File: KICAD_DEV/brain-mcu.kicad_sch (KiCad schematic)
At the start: 14 parts, among them SW1 SW_Push, U1 STM32H743VITx

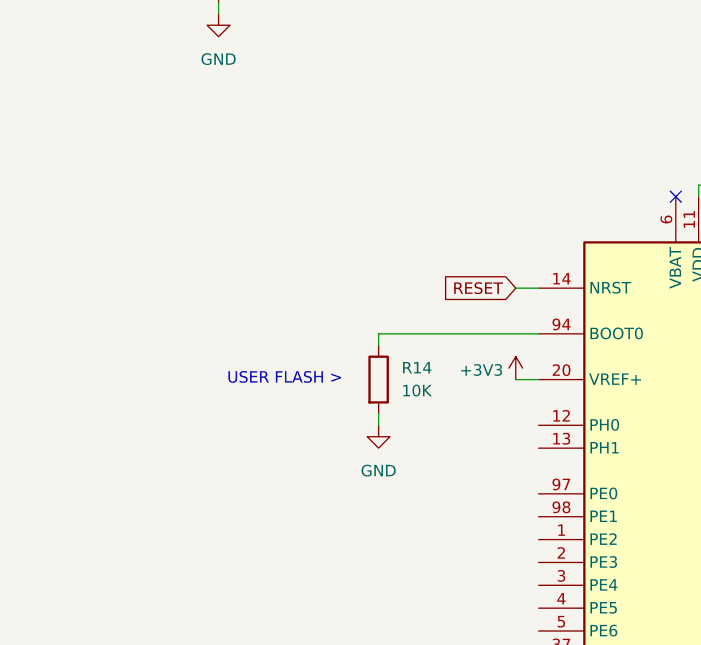
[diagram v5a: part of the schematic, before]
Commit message: added the boot button
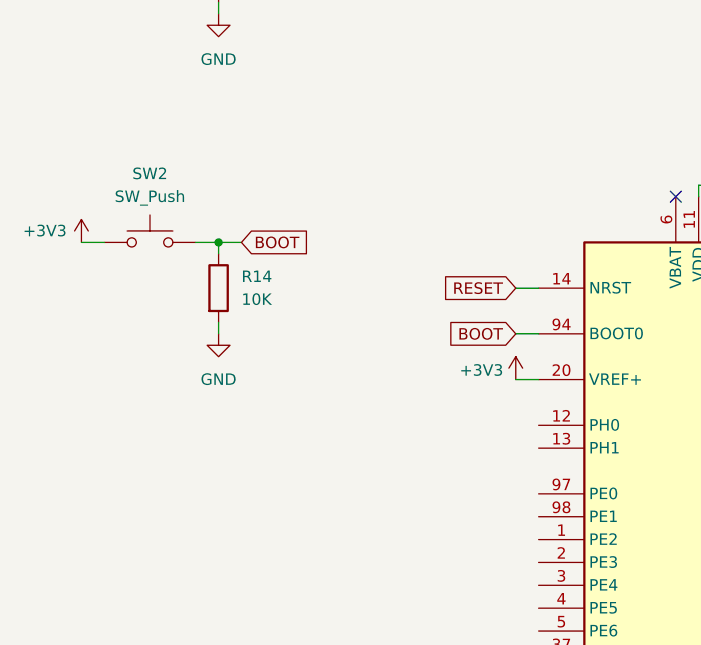
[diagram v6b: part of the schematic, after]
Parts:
- added SW2: SW_Push, symbol Switch:SW_Push
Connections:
- net +3V3: now also SW2.1
- net BOOT: now reaches R14.1, U1.94 (BOOT0)
- net BOOT: now also SW2.2
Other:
- note removed: "USER FLASH >"
- moved on the sheet: R14
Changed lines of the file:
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@@
 	(generator_version "9.0")
 	(paper "A3")
-	(text "USER FLASH >"
-		(exclude_from_sim no)
-		(at 171.196 111.76 0)
-		(effects
-			(font
-				(size 1.27 1.27)
-			)
-		)
-	)
 	(junction
 		(at 219.71 90.17)
@@
 		(color 0 0 0 0)
 	)
+	(junction
+		(at 163.83 96.52)
+		(diameter 0)
+		(color 0 0 0 0)
+	)
 	(no_connect
 		(at 214.63 91.44)
@@
 	(wire
 		(pts
+			(xy 148.59 96.52) (xy 151.13 96.52)
+		)
+		(stroke
+			(width 0)
+			(type default)
+		)
+	)
+	(wire
+		(pts
 			(xy 198.12 210.82) (xy 199.39 210.82)
 		)
@@
 	(wire
 		(pts
-			(xy 181.61 107.95) (xy 181.61 106.68)
+			(xy 163.83 97.79) (xy 163.83 96.52)
 		)
 		(stroke
@@
 	(wire
 		(pts
-			(xy 181.61 106.68) (xy 199.39 106.68)
-		)
-		(stroke
-			(width 0)
-			(type default)
-		)
-	)
-	(wire
-		(pts
 			(xy 208.28 55.88) (xy 208.28 57.15)
 		)
@@
 	(wire
 		(pts
+			(xy 196.85 106.68) (xy 199.39 106.68)
+		)
+		(stroke
+			(width 0)
+			(type default)
+		)
+	)
+	(wire
+		(pts
 			(xy 238.76 55.88) (xy 238.76 57.15)
 		)
@@
 	(wire
 		(pts
+			(xy 161.29 96.52) (xy 163.83 96.52)
+		)
+		(stroke
+			(width 0)
+			(type default)
+		)
+	)
+	(wire
+		(pts
 			(xy 148.59 60.96) (xy 151.13 60.96)
 		)
@@
 	(wire
 		(pts
+			(xy 163.83 96.52) (xy 166.37 96.52)
+		)
+		(stroke
+			(width 0)
+			(type default)
+		)
+	)
+	(wire
+		(pts
 			(xy 223.52 53.34) (xy 223.52 55.88)
 		)
@@
 	(wire
 		(pts
-			(xy 181.61 116.84) (xy 181.61 115.57)
+			(xy 163.83 106.68) (xy 163.83 105.41)
 		)
 		(stroke
@@
 		)
 	)
+	(global_label "BOOT"
+		(shape input)
+		(at 166.37 96.52 0)
+		(fields_autoplaced yes)
+		(effects
+			(font
+				(size 1.27 1.27)
+			)
+			(justify left)
+		)
+		(property "Intersheetrefs" "${INTERSHEET_REFS}"
+			(at 174.2538 96.52 0)
+			(effects
+				(font
+					(size 1.27 1.27)
+				)
+				(justify left)
+				(hide yes)
+			)
+		)
+	)
+	(global_label "BOOT"
+		(shape input)
+		(at 196.85 106.68 180)
+		(fields_autoplaced yes)
+		(effects
+			(font
+				(size 1.27 1.27)
+			)
+			(justify right)
+		)
+		(property "Intersheetrefs" "${INTERSHEET_REFS}"
+			(at 188.9662 106.68 0)
+			(effects
+				(font
+					(size 1.27 1.27)
+				)
+				(justify right)
+				(hide yes)
+			)
+		)
+	)
 	(symbol
 		(lib_id "Device:C")
@@
 	)
 	(symbol
+		(lib_id "power:+3V3")
+		(at 148.59 96.52 0)
+		(unit 1)
+		(exclude_from_sim no)
+		(in_bom yes)
+		(on_board yes)
+		(dnp no)
+		(property "Reference" "#PWR043"
+			(at 148.59 100.33 0)
+			(effects
+				(font
+					(size 1.27 1.27)
+				)
+				(hide yes)
+			)
+		)
+		(property "Value" "+3V3"
+			(at 144.526 95.25 0)
+			(effects
+				(font
+					(size 1.27 1.27)
+				)
+			)
+		)
+		(property "Footprint" ""
+			(at 148.59 96.52 0)
+			(effects
+				(font
+					(size 1.27 1.27)
+				)
+				(hide yes)
+			)
+		)
+		(property "Datasheet" ""
+			(at 148.59 96.52 0)
+			(effects
+				(font
+					(size 1.27 1.27)
+				)
+				(hide yes)
+			)
+		)
+		(property "Description" "Power symbol creates a global label with name \"+3V3\""
+			(at 148.59 96.52 0)
+			(effects
+				(font
+					(size 1.27 1.27)
+				)
+				(hide yes)
+			)
+		)
+		(pin "1"
+		)
+		(instances
+			(project ""
+				(path "/28389848-e686-45d1-8788-e912d76b51d3/e89d2a57-06d5-4f43-8b58-178aa33298cf"
+					(reference "#PWR043")
+					(unit 1)
+				)
+			)
+		)
+	)
+	(symbol
 		(lib_id "Switch:SW_Push")
 		(at 156.21 60.96 0)
@@
 	(symbol
 		(lib_id "Device:R")
-		(at 181.61 111.76 0)
+		(at 163.83 101.6 0)
 		(unit 1)
 		(exclude_from_sim no)
@@
 		(fields_autoplaced yes)
 		(property "Reference" "R14"
-			(at 184.15 110.4899 0)
+			(at 166.37 100.3299 0)
 			(effects
 				(font
@@
 		)
 		(property "Value" "10K"
-			(at 184.15 113.0299 0)
-			(effects
-				(font
-					(size 1.27 1.27)
-				)
-				(justify left)
-			)
-		)
-		(property "Footprint" ""
-			(at 179.832 111.76 90)
+			(at 166.37 102.8699 0)
+			(effects
+				(font
+					(size 1.27 1.27)
+				)
+				(justify left)
+			)
+		)
+		(property "Footprint" ""
+			(at 162.052 101.6 90)
 			(effects
 				(font
@@
 		)
 		(property "Datasheet" "~"
-			(at 181.61 111.76 0)
+			(at 163.83 101.6 0)
 			(effects
 				(font
@@
 		)
 		(property "Description" "Resistor"
-			(at 181.61 111.76 0)
+			(at 163.83 101.6 0)
 			(effects
 				(font
@@
 	)
 	(symbol
+		(lib_id "Switch:SW_Push")
+		(at 156.21 96.52 0)
+		(unit 1)
+		(exclude_from_sim no)
+		(in_bom yes)
+		(on_board yes)
+		(dnp no)
+		(fields_autoplaced yes)
+		(property "Reference" "SW2"
+			(at 156.21 88.9 0)
+			(effects
+				(font
+					(size 1.27 1.27)
+				)
+			)
+		)
+		(property "Value" "SW_Push"
+			(at 156.21 91.44 0)
+			(effects
+				(font
+					(size 1.27 1.27)
+				)
+			)
+		)
+		(property "Footprint" ""
+			(at 156.21 91.44 0)
+			(effects
+				(font
+					(size 1.27 1.27)
+				)
+				(hide yes)
+			)
+		)
+		(property "Datasheet" "~"
+			(at 156.21 91.44 0)
+			(effects
+				(font
+					(size 1.27 1.27)
+				)
+				(hide yes)
+			)
+		)
+		(property "Description" "Push button switch, generic, two pins"
+			(at 156.21 96.52 0)
+			(effects
+				(font
+					(size 1.27 1.27)
+				)
+				(hide yes)
+			)
+		)
+		(pin "1"
+		)
+		(pin "2"
+		)
+		(instances
+			(project ""
+				(path "/28389848-e686-45d1-8788-e912d76b51d3/e89d2a57-06d5-4f43-8b58-178aa33298cf"
+					(reference "SW2")
+					(unit 1)
+				)
+			)
+		)
+	)
+	(symbol
 		(lib_id "Device:C")
 		(at 223.52 60.96 0)
@@
 	(symbol
 		(lib_id "power:GND")
-		(at 181.61 116.84 0)
+		(at 163.83 106.68 0)
 		(unit 1)
 		(exclude_from_sim no)
@@
 		(fields_autoplaced yes)
 		(property "Reference" "#PWR042"
-			(at 181.61 123.19 0)
+			(at 163.83 113.03 0)
 			(effects
 				(font
@@
 		)
 		(property "Value" "GND"
-			(at 181.61 121.92 0)
-			(effects
-				(font
-					(size 1.27 1.27)
-				)
-			)
-		)
-		(property "Footprint" ""
-			(at 181.61 116.84 0)
+			(at 163.83 111.76 0)
+			(effects
+				(font
+					(size 1.27 1.27)
+				)
+			)
+		)
+		(property "Footprint" ""
+			(at 163.83 106.68 0)
 			(effects
 				(font
@@
 		)
 		(property "Datasheet" ""
-			(at 181.61 116.84 0)
+			(at 163.83 106.68 0)
 			(effects
 				(font
@@
 		)
 		(property "Description" "Power symbol creates a global label with name \"GND\" , ground"
-			(at 181.61 116.84 0)
-			(effects
-				(font
+			(at 163.83 106.68 0)
+			(effects
+				(font

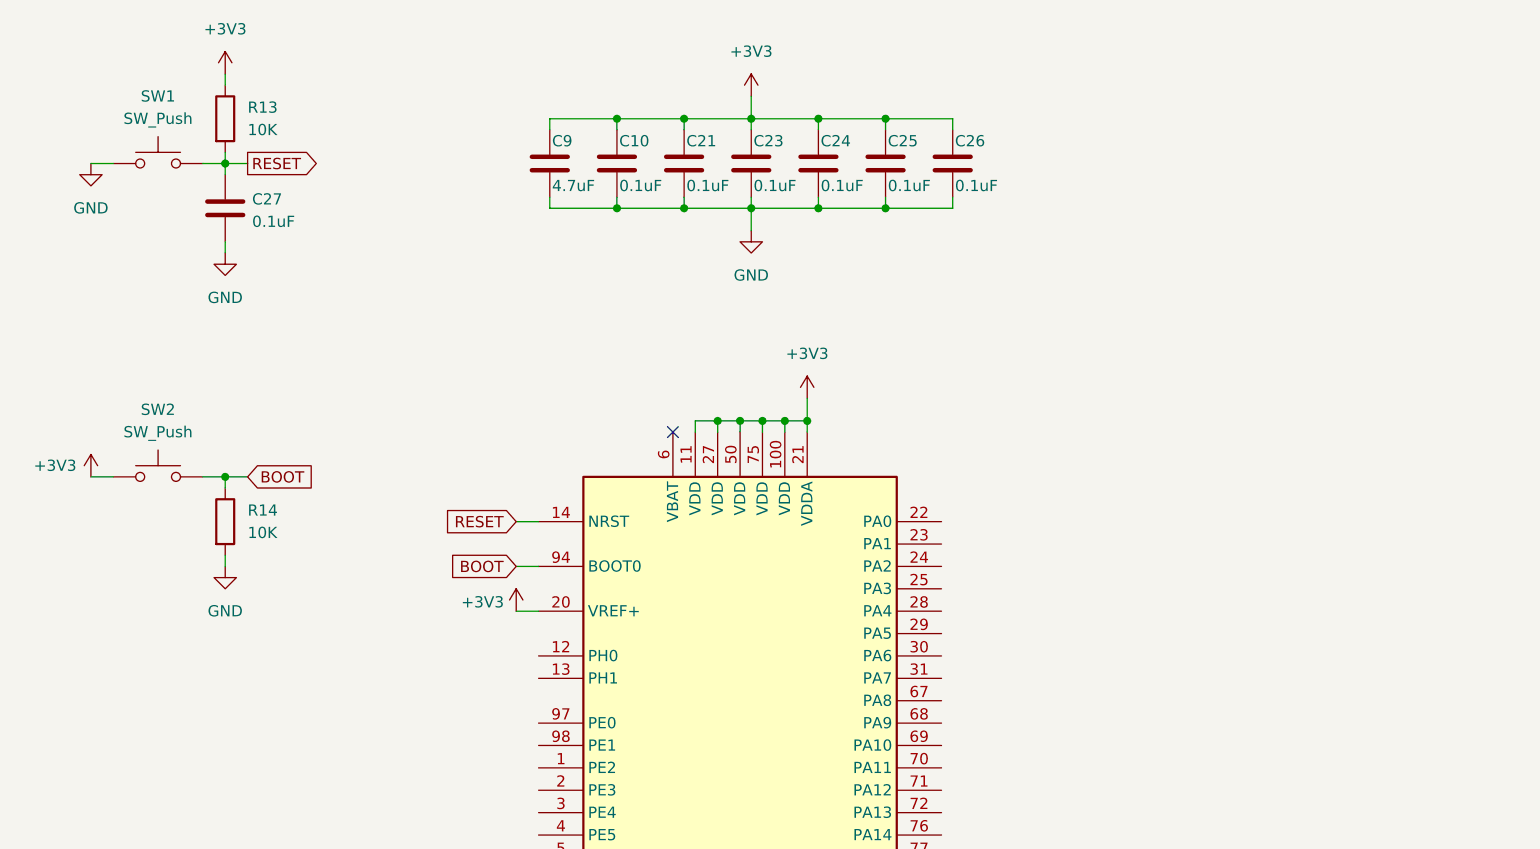
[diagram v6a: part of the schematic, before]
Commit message: adding the 8mhz crystal
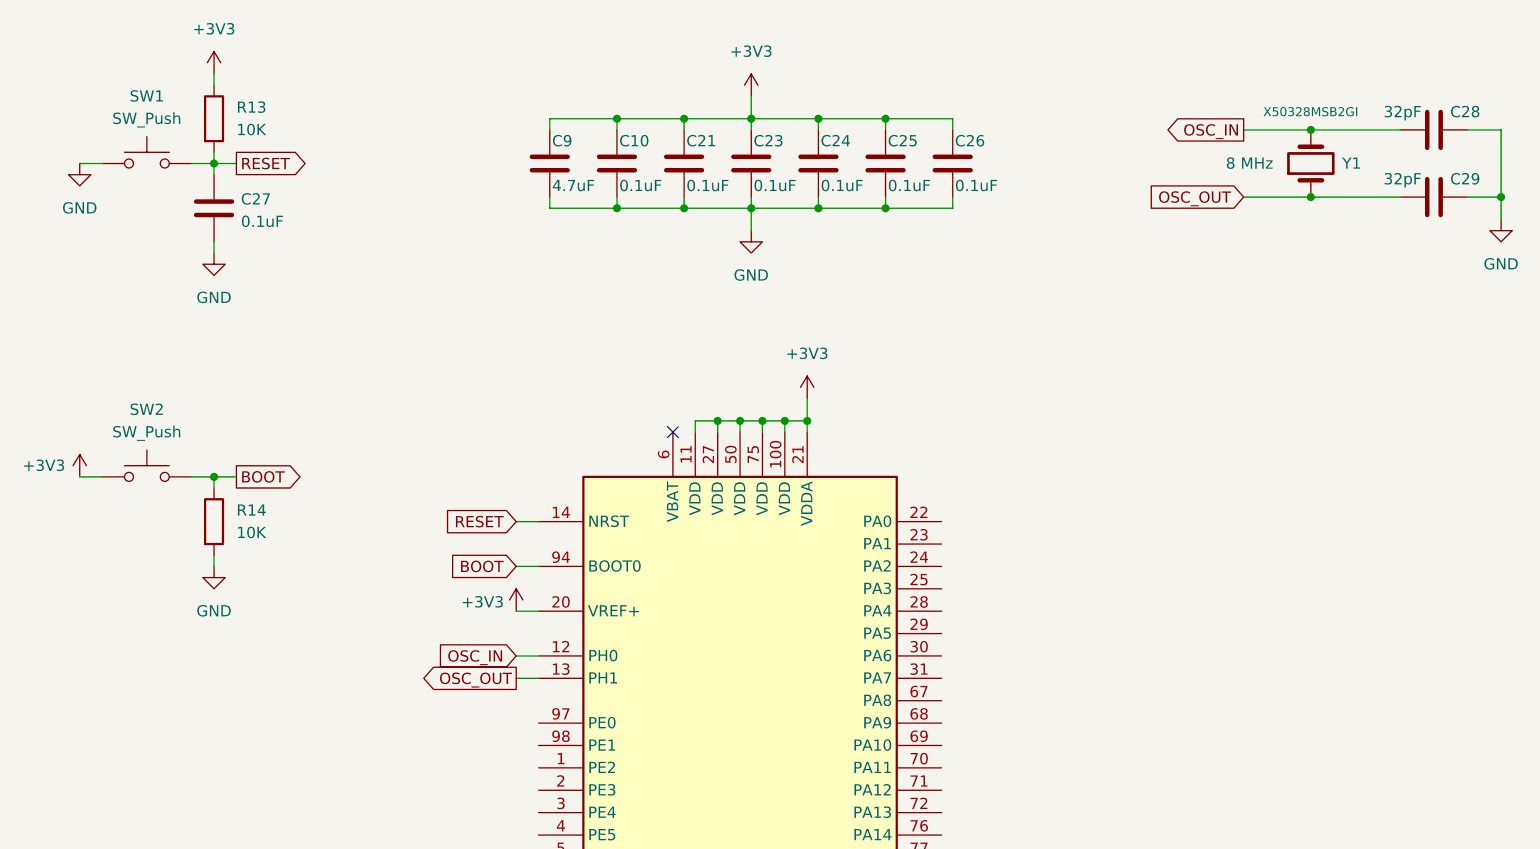
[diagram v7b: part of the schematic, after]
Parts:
- added C28, C29: 32pF, symbol Device:C
- added Y1: 8 MHz, symbol Device:Crystal
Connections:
- net GND: now also C28.2, C29.2
- net OSC_IN: now reaches U1.12 (PH0)
- net OSC_IN: now also C28.1, Y1.2
- net OSC_OUT: now reaches U1.13 (PH1)
- net OSC_OUT: now also C29.1, Y1.1
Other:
- moved on the sheet: C27, R13, R14, SW1, SW2

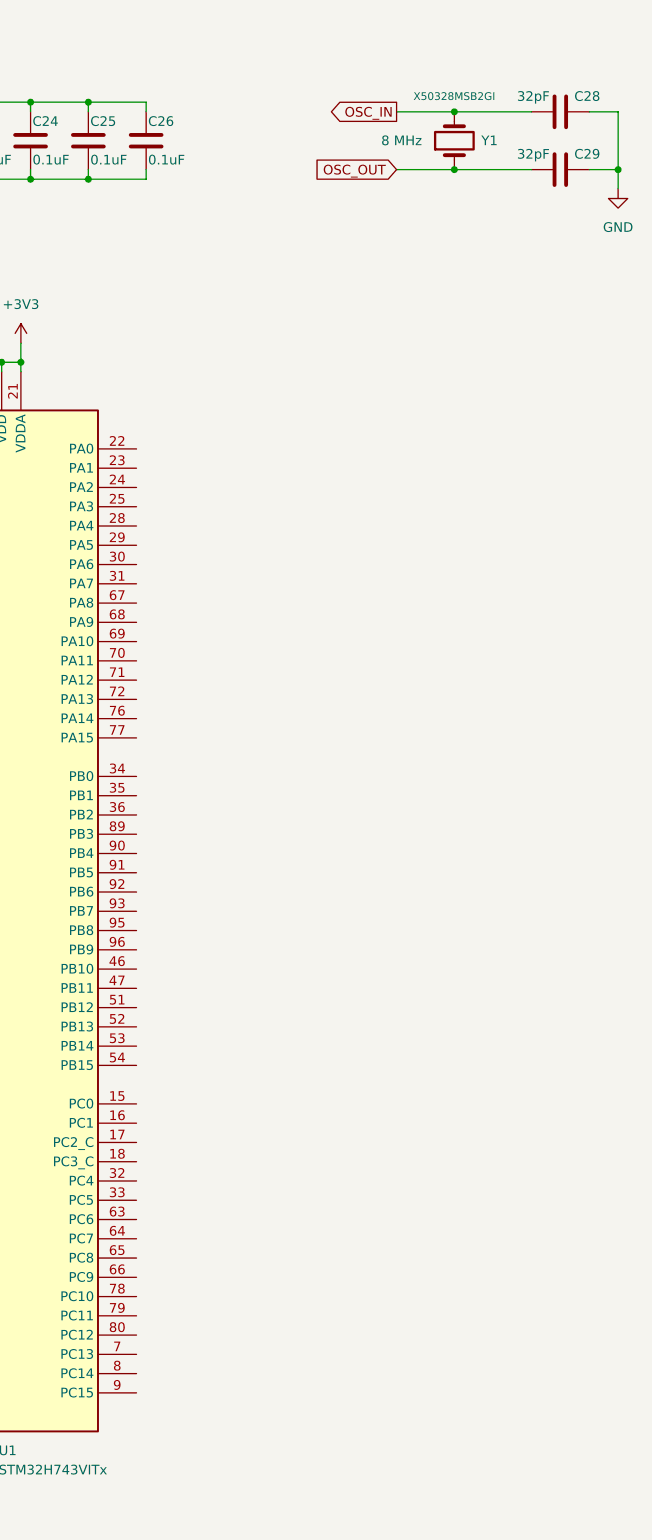
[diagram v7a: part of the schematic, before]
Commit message: adding the 32.768KHz crystal!
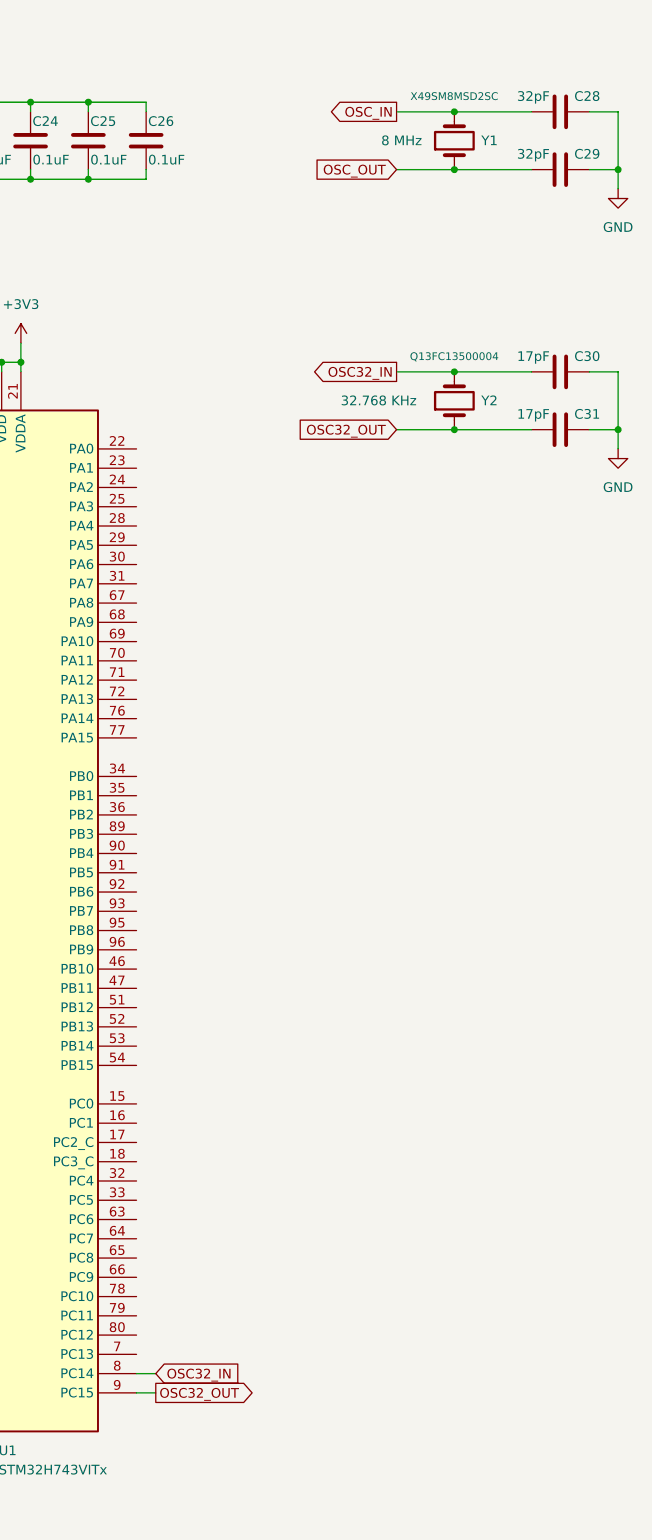
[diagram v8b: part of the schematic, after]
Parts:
- added C30, C31: 17pF, symbol Device:C
- added Y2: 32.768 KHz, symbol Device:Crystal
- Y1: Part X50328MSB2GI -> X49SM8MSD2SC
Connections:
- net GND: now also C30.2, C31.2
- net OSC32_IN: now reaches U1.8 (PC14)
- net OSC32_IN: now also C30.1, Y2.2
- net OSC32_OUT: now reaches U1.9 (PC15)
- net OSC32_OUT: now also C31.1, Y2.1
